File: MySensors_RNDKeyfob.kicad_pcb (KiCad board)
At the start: 2 copper layers, 27 x 42.9 mm, 17 parts, among them P1 CONN_01X01, P2 CONN_02X03, SW1 SW_SPST, SW2 SW_SPST, SW3 SW_SPST, SW4 SW_SPST, SW5 SW_SPST, U1 ATSHA204A, U2 RFM69HCW, U3 ATMEGA328P-MU

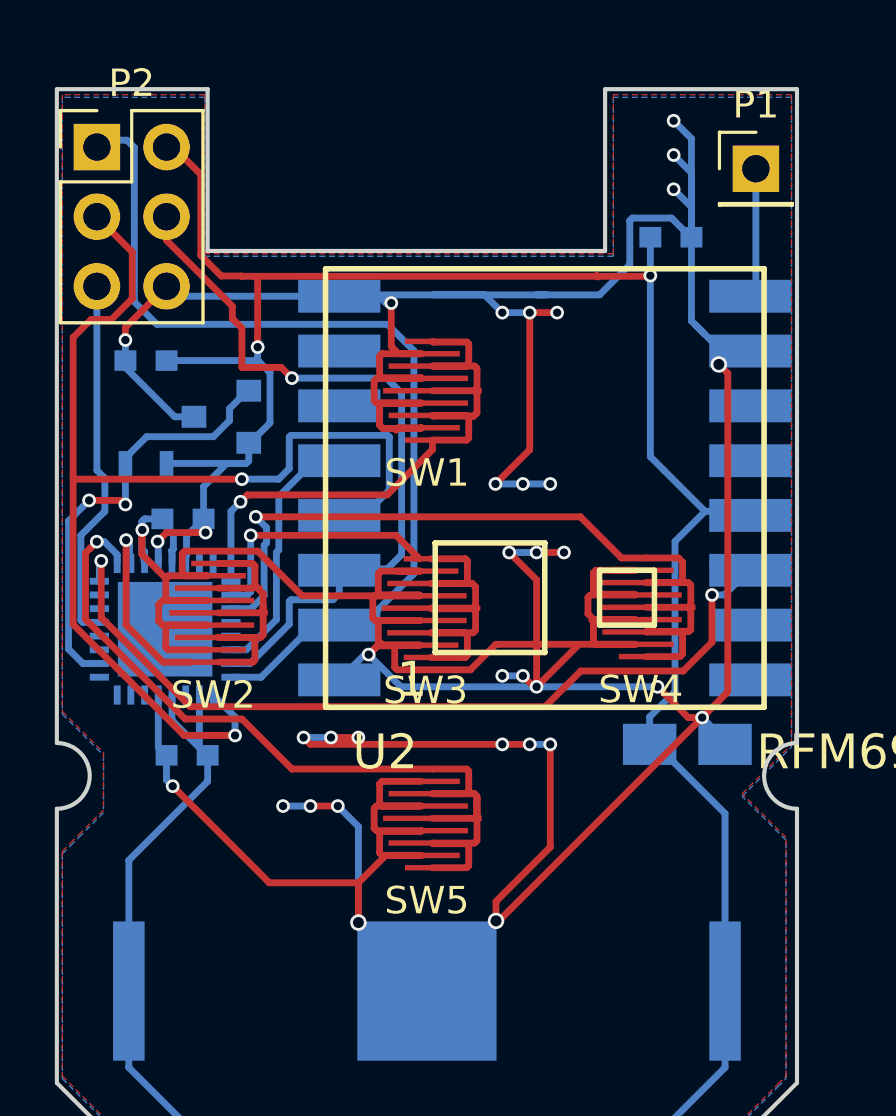
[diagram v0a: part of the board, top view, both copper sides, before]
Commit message: Turned ICSP header to backside, improved rubber button pads
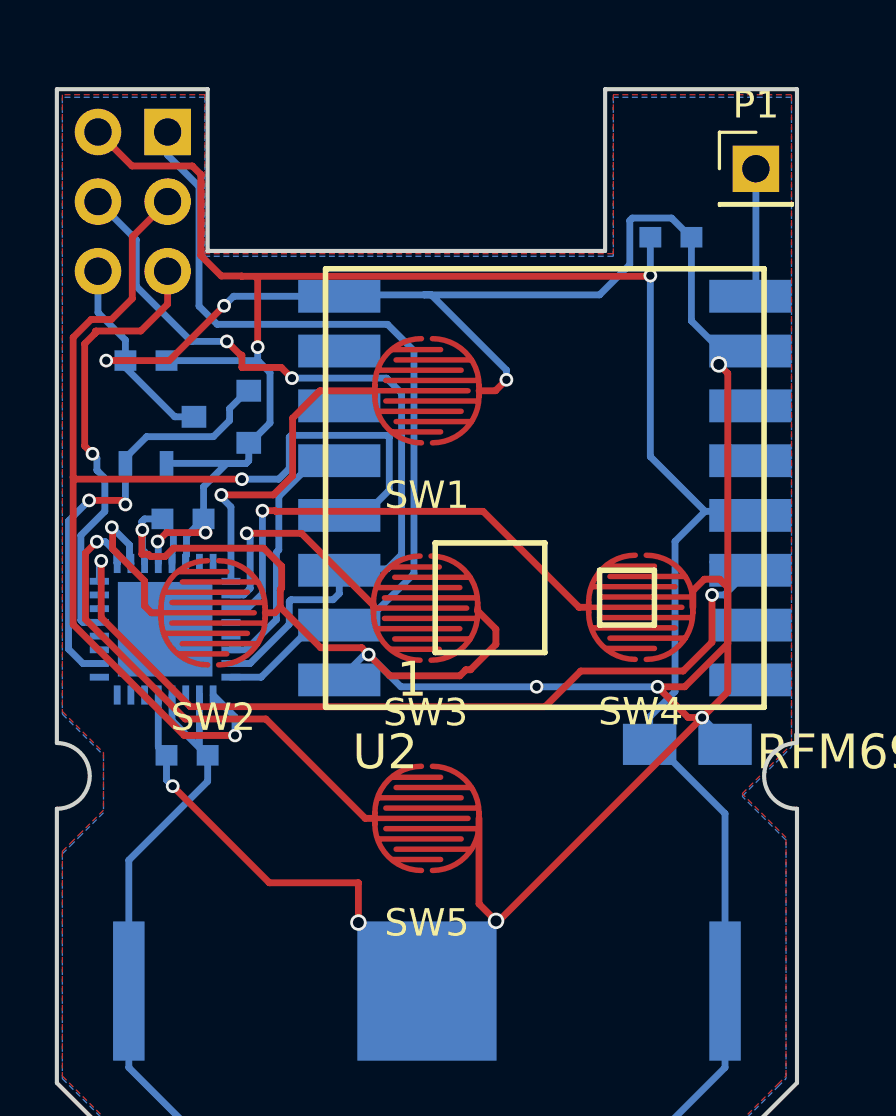
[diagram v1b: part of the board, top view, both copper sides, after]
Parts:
- P2: moved to B.Cu
- moved P2 2.64 mm to (190.5, 58.7), turned to 180 degrees
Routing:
- net GND: track 259.8 -> 143.0 mm, vias 34 -> 12
- net /D6: track 24.3 -> 8.68 mm
- net /D3: track 33.3 -> 18.2 mm
- net /D7: track 32.8 -> 17.8 mm
- net /D4: track 19.8 -> 5.74 mm
- net /D5: track 24.7 -> 11.7 mm
- net /RESET: track 13.4 -> 16.3 mm, vias 0 -> 1
- net /MISO: track 34.4 -> 31.7 mm
- net /VCC: track 123.9 -> 126.4 mm
- net /MOSI: track 27.6 -> 29.9 mm, vias 1 -> 2
- net /SCK: track 44.4 -> 45.0 mm
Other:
- net class Default: clearance 0.16 -> 0.17
- rule trace_clearance: 0.16 -> 0.17

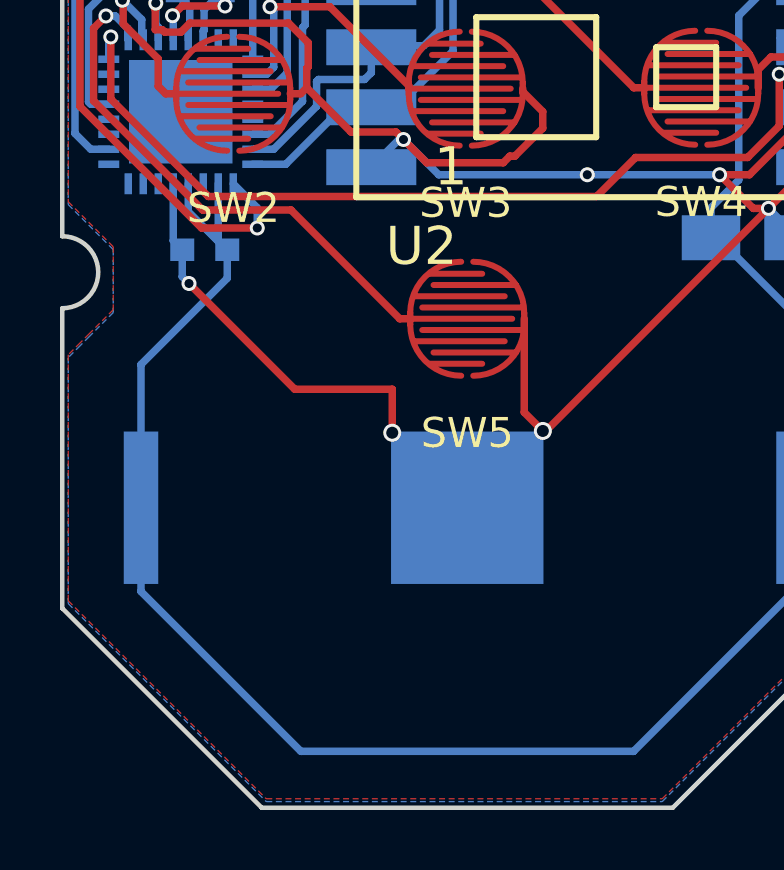
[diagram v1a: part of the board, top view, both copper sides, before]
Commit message: Added RGB LED
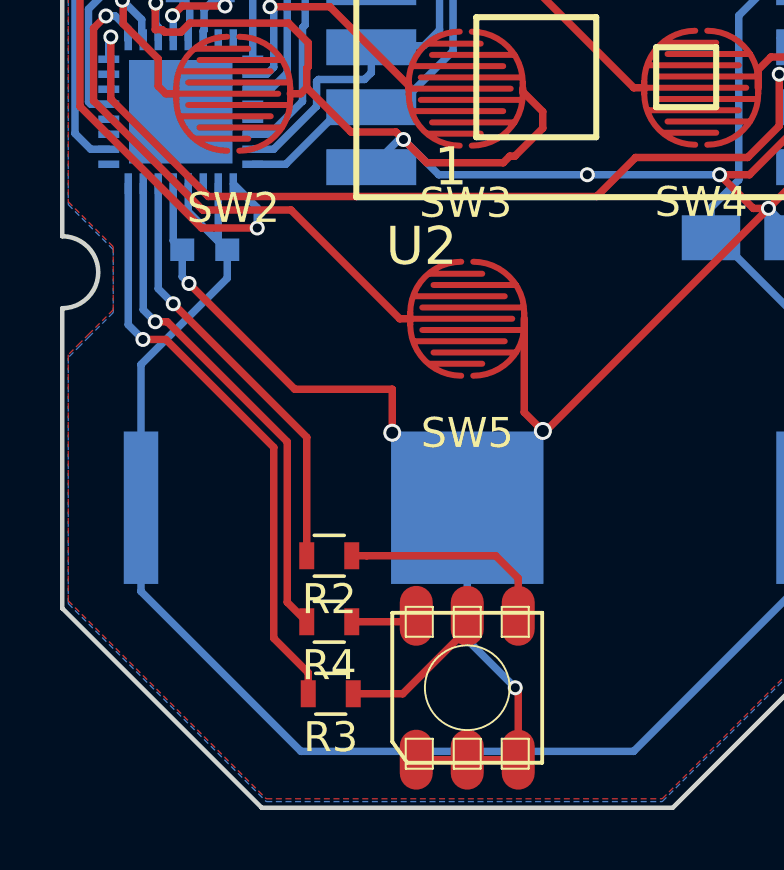
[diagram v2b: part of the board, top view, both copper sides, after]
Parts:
- added D1: LED_RGB, SparkFun-LED:LED-TRICOLOR-5050, F.Cu at (200.0, 96.0)
- added R2: R, Resistors_SMD:R_0603, F.Cu at (195.4, 91.6)
- added R3: R, Resistors_SMD:R_0603, F.Cu at (195.4, 96.2)
- added R4: R, Resistors_SMD:R_0603, F.Cu at (195.4, 93.8)
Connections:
- U2 pad 11: Net-(U2-Pad11) -> (no net)
- U2 pad 12: Net-(U2-Pad12) -> (no net)
- U2 pad 15: Net-(U2-Pad15) -> (no net)
- U2 pad 16: Net-(U2-Pad16) -> (no net)
- U2 pad 6: Net-(U2-Pad6) -> (no net)
- U2 pad 7: Net-(U2-Pad7) -> (no net)
- U3 pad 12: /D8 -> (no net)
- U3 pad 13: /D9 -> (no net)
- U3 pad 19: /A6 -> (no net)
- U3 pad 25: /A2 -> (no net)
- U3 pad 27: /A4 -> (no net)
- U3 pad 28: /A5 -> (no net)
- U3 pad 30: /RXI -> (no net)
- U3 pad 31: /TXO -> (no net)
- U3 pad 7: /D20 -> (no net)
- U3 pad 8: /D21 -> (no net)
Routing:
- net /A1: track 0.00 -> 19.9 mm, vias 0 -> 1
- net /A0: track 0.00 -> 17.1 mm, vias 0 -> 1
- net /A7: track 0.00 -> 14.5 mm, vias 0 -> 1
- net GND: track 143.0 -> 155.5 mm, vias 12 -> 13
- net Net-(D1-Pad4): track 0.00 -> 7.11 mm
- net Net-(D1-Pad5): track 0.00 -> 5.14 mm
- net Net-(D1-Pad6): track 0.00 -> 2.23 mm

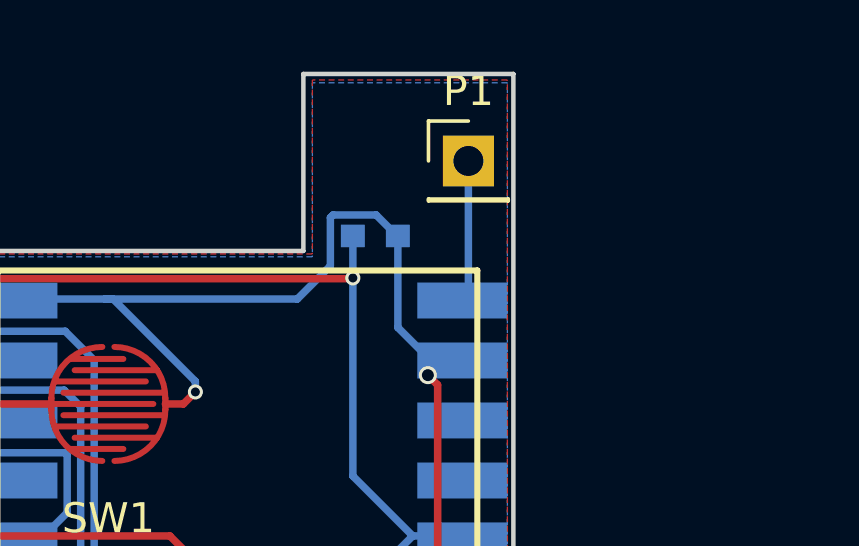
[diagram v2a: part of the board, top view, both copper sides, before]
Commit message: Changed antenna net impedance to 50 Ohm
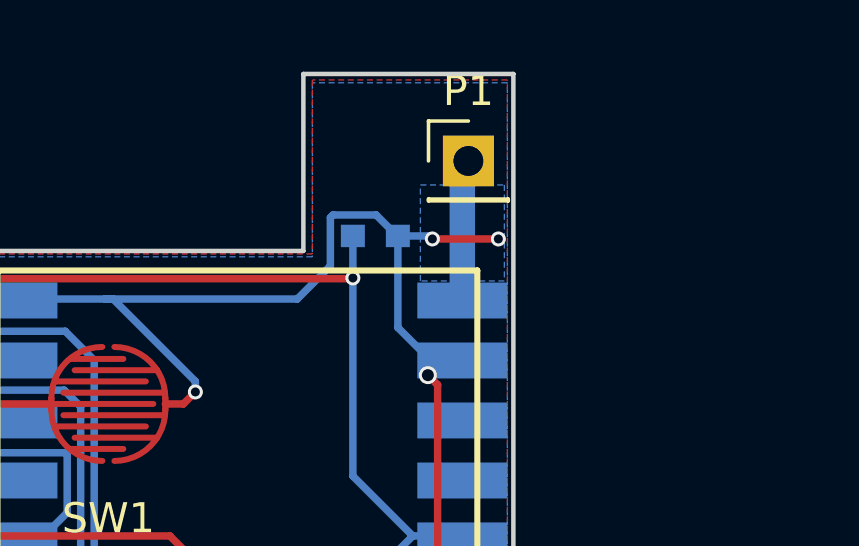
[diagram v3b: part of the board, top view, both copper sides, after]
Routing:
- net GND: track 155.5 -> 158.9 mm, vias 13 -> 15
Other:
- net class Antenna added: clearance 0.2, trace_width 0.85, via_dia 0.5, via_drill 0.3
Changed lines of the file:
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@@
     (links 58)
     (no_connects 0)
-    (area 186.424999 57.024999 213.575001 100.075001)
+    (area 176.371667 55.385 222.419697 100.245001)
     (thickness 1.6)
     (drawings 20)
-    (tracks 389)
+    (tracks 395)
     (zones 0)
     (modules 21)
@@
     (add_net /A3)
     (add_net /A7)
-    (add_net /ANT)
     (add_net /D10)
     (add_net /D2)
@@
     (add_net "Net-(D1-Pad5)")
     (add_net "Net-(D1-Pad6)")
+  )
+  (net_class Antenna ""
+    (clearance 0.2)
+    (trace_width 0.85)
+    (via_dia 0.5)
+    (via_drill 0.3)
+    (uvia_dia 0.3)
+    (uvia_drill 0.1)
+    (add_net /ANT)
   )
   (module SparkFun-RF:RFM69HCW-XXXS2 (layer B.Cu)
@@
   (segment (start 210.580075 74.49974) (end 210.425009 74.344674) (width 0.25) (layer B.Cu) (net 7) (status 30))
   (segment (start 211.49808 74.49974) (end 210.580075 74.49974) (width 0.25) (layer B.Cu) (net 7) (status 30))
-  (segment (start 212 60) (end 212 64.45038) (width 0.25) (layer B.Cu) (net 8) (status 30))
+  (segment (start 211.79808 64.6523) (end 211.79808 60.20192) (width 0.85) (layer B.Cu) (net 8))
+  (segment (start 211.79808 60.20192) (end 212 60) (width 0.85) (layer B.Cu) (net 8))
   (segment (start 212 64.45038) (end 211.79808 64.6523) (width 0.25) (layer B.Cu) (net 8) (status 30))
   (segment (start 187.956586 73.606587) (end 188.269233 73.606587) (width 0.25) (layer B.Cu) (net 9))
@@
   (segment (start 189.774999 69.775001) (end 189 70.55) (width 0.25) (layer B.Cu) (net 14) (status 20))
   (segment (start 189 70.55) (end 189 70.75) (width 0.25) (layer B.Cu) (net 14) (status 30))
+  (segment (start 210.8 62.6) (end 213 62.6) (width 0.25) (layer F.Cu) (net 15))
+  (via (at 213 62.6) (size 0.5) (drill 0.3) (layers F.Cu B.Cu) (net 15))
+  (segment (start 209.65 62.5) (end 210.7 62.5) (width 0.25) (layer B.Cu) (net 15))
+  (via (at 210.8 62.6) (size 0.5) (drill 0.3) (layers F.Cu B.Cu) (net 15))
+  (segment (start 210.7 62.5) (end 210.8 62.6) (width 0.25) (layer B.Cu) (net 15))
   (segment (start 201.6 96) (end 200 94.4) (width 0.25) (layer B.Cu) (net 15))
   (segment (start 200 94.4) (end 200 90) (width 0.25) (layer B.Cu) (net 15))
@@
       )
     )
+  )
+  (zone (net 15) (net_name GND) (layer B.Cu) (hatch edge 0.508)
+    (connect_pads (clearance 0.2))
+    (min_thickness 0.254)
+    (fill yes (arc_segments 16) (thermal_gap 0.508) (thermal_bridge_width 0.508))
+    (polygon
+      (pts
+        (xy 210.4 60.8) (xy 213.2 60.8) (xy 213.2 64) (xy 210.4 64)
+      )
+    )

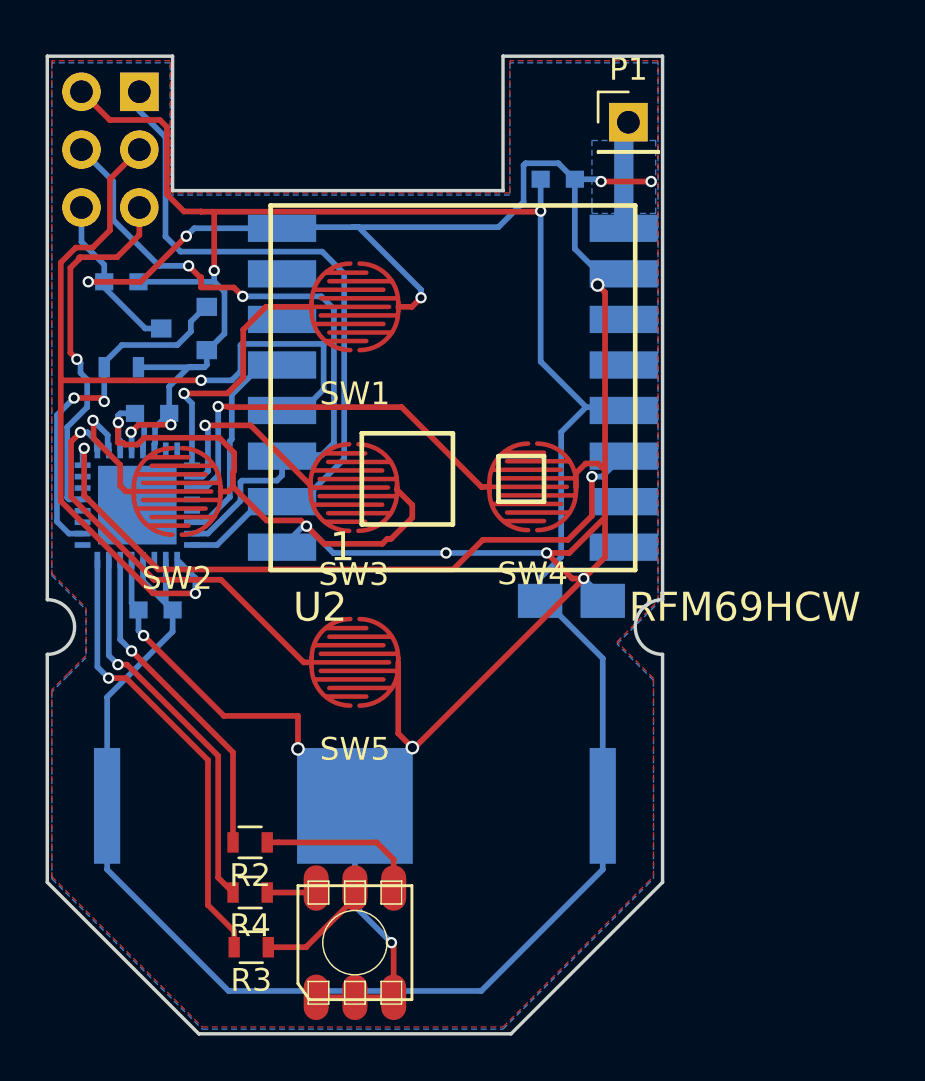
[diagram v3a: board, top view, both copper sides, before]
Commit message: Fine tuning with antenna, trace distances to v-cuts, position of RGB LED
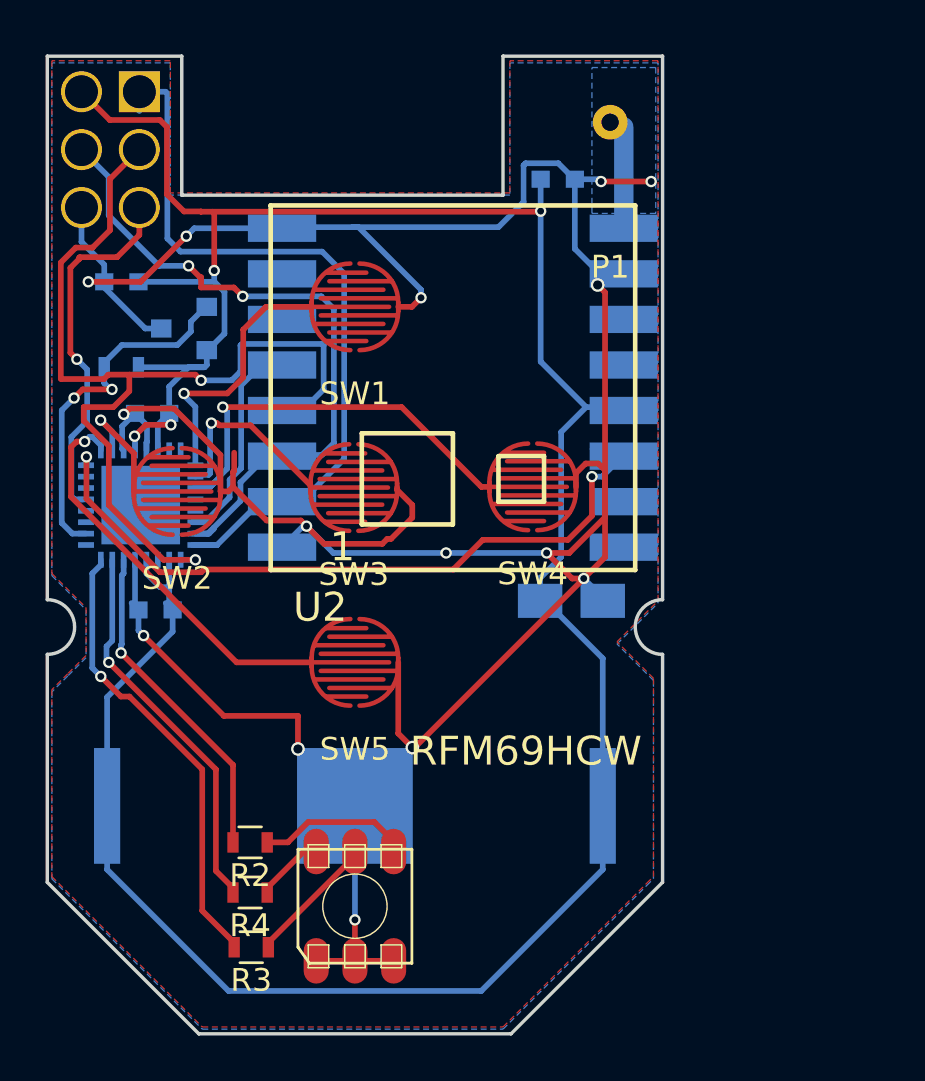
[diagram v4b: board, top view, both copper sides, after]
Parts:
- P1: footprint Pin_Headers:Pin_Header_Straight_1x01_Pitch2.54mm -> parts:868MHz_Spring_Antenna
- moved D1 1.60 mm to (200.0, 94.4)
- moved P1 0.80 mm to (211.2, 60.0)
- moved U3 0.15 mm to (190.6, 76.8)
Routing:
- net /MISO: track 31.7 -> 34.2 mm
- net GND: track 158.9 -> 157.4 mm
- net /D7: track 17.8 -> 19.2 mm
- net /SCK: track 45.0 -> 43.6 mm
- net /VCC: track 126.4 -> 125.5 mm
- net Net-(D1-Pad6): track 2.23 -> 3.01 mm
- net Net-(D1-Pad5): track 5.14 -> 5.77 mm
- net /D3: track 18.2 -> 17.6 mm
- net /D2: track 32.1 -> 31.6 mm
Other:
- outline, holes or cut-outs redrawn
